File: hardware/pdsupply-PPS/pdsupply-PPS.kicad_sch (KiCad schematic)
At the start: 36 parts

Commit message: added a buck boost
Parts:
- removed C?: 0.1uF, symbol Device:C_Small
- removed C?: 10uF X5R 0805, symbol Device:C_Small
- removed C? (x4): 1uF, symbol Device:C_Small
- removed C? (x2): 12pF, symbol Device:C_Small
- removed Q?: STL6P3LLH6, TRANS_STL6P3LLH6, symbol STL6P3LLH6:STL6P3LLH6
- removed R?: 100, symbol Device:R_Small_US
- removed R? (x3): 100k, symbol Device:R_Small_US
- removed R? (x2): 1K, symbol Device:R_Small_US
- removed R?: 76.8k, symbol Device:R_Small_US
- removed R?: 22K, symbol Device:R_Small_US
- removed R?: 23.7k, symbol Device:R_Small_US
- removed U?: STUSB4500QTR, Package_DFN_QFN:QFN-24-1EP_4x4mm_P0.5mm_EP2.7x2.7mm, symbol Interface_USB:STUSB4500QTR
- removed U?: LTM8074IY, BGA25C65P5X5_400X400X198N, symbol LTM8074IY_PBF:LTM8074IY#PBF_MIRRORED
- removed Y?: Crystal, symbol Device:Crystal_GND24
- added C?: 22uF, symbol Device:C_Polarized_Small
- added C? (x2): 0.1uF, symbol Device:C_Small
- added C? (x3): 10uF, symbol Device:C_Small
- added FB? (x2): 1000Ω AT 100MHz, symbol Device:FerriteBead_Small
- added FB?: 300Ω AT 100MHz, symbol Device:FerriteBead_Small
- added IC?: FPF2895UCX, BGA24C40P4X6_167X260X61, symbol FPF2895UCX:FPF2895UCX
- added IC?: LTM8083EY#PBF, BGA49C80P7X7_625X625X242, symbol LTM8083EY#PBF:LTM8083EY#PBF
- added JP? (x2): Jumper_2_Open, symbol Jumper:Jumper_2_Open
- added R?: 200k, symbol Device:R_Small_US
- added R?: 22k, symbol Device:R_Small_US
- added R?: 50.6k, symbol Device:R_Small_US
- added R?: 270k, symbol Device:R_Small_US
- added R?: 40.2k, symbol Device:R_Small_US
- added U?: FUSB307BMPX, Package_DFN_QFN:WQFN-16-1EP_3x3mm_P0.5mm_EP1.75x1.75mm, symbol Interface_USB:FUSB307BMPX
- added X?: XO91, Oscillator:Oscillator_SMD_EuroQuartz_XO91-4Pin_7.0x5.0mm, symbol Oscillator:XO91
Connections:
- net +3V3: now also D?.1 (VDD), D?.1 (VDD), C?.1, FB?.2, X?.1 (EN), X?.4 (V+)
- net GND: now also D?.6 (GND), D?.6 (GND), C?.2, C?.2, C?.2, C?.2, C?.2, C?.2, IC?.A1 (GND_1), IC?.A2 (GND_2), IC?.A3 (GND_3), IC?.A7 (TST2), IC?.B1 (GND_4), IC?.B2 (GND_5), IC?.B3 (GND_6), IC?.B7 (OVLO), IC?.C1 (GND_7), IC?.C2 (GND_8), IC?.C3 (GND_9), IC?.C4 (GND_10), IC?.C5 (GND_11), IC?.D1 (GND_12), IC?.D2 (GND_13), IC?.D3 (GND_14), IC?.D4 (GND_15), IC?.D5 (GND_16), IC?.D7 (GND_17), IC?.E1 (GND_18), IC?.E2 (GND_19), IC?.E3 (GND_20), IC?.E4 (GND_21), IC?.E5 (GND_22), IC?.F1 (GND_23), IC?.F2 (GND_24), IC?.G1 (GND_25), IC?.G2 (GND_26), IC?.G6 (SYNC), R?.2, R?.2, R?.2, X?.2 (GND)
- net VBUS: now also C?.1, C?.1, FB?.1, FB?.1
- net at R?.2, U?.7 (UD+): now also JP?.1 (A)
- net SPI1_DATA: now reaches U?.13 (PA7)
- net SPI1_DATA: now also D?.4 (SDI)
- net USB_DM: now reaches U?.21 (PA11)
- net USB_DM: now also U?.11 (DD-), JP?.2 (B)
- net USB_DP: now reaches U?.22 (PA12)
- net USB_DP: now also U?.10 (DD+), JP?.2 (B)
- net SPI3_CLK: now reaches U?.26 (PB3)
- net SPI3_CLK: now also D?.5 (CKI)
- net SPI3_DATA: now reaches U?.28 (PB5)
- net SPI3_DATA: now also D?.4 (SDI)
- net at U?.6 (PA0): now also X?.3 (OUT)
- net SPI1_CLK: now reaches U?.7 (PA1)
- net SPI1_CLK: now also D?.5 (CKI)
- net at R?.1, U?.6 (UD-): now also JP?.1 (A)
- new net: C?.1, C?.1, FB?.2, FB?.2, IC?.A4 (VIN_1), IC?.A5 (VIN_2), IC?.A6 (SVIN), IC?.B4 (VIN_3), IC?.B5 (VIN_4), R?.1
- new net: IC?.B6 (EN/UVLO), R?.1, R?.2
- new net: U?.15 (GND), U?.17 (GND)
- new net: IC?.F7 (FB), R?.1, R?.2
- new net: C?.1, FB?.1, IC?.F3 (ISN), IC?.F4 (VOUT_1), IC?.F5 (VOUT_2), IC?.G3 (ISP), IC?.G4 (VOUT_3), IC?.G5 (VOUT_4), R?.1
- new net: IC?.E7 (RT), R?.1
- no-connect marks 19 -> 20
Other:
- note added: "Compliant with CISPR25 Class 5 Limits"
- moved on the sheet: C?, D?, PH?, R?, U?

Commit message: minor changes
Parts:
- removed D? (x2): APA102-2020, LED_SMD:LED-APA102-2020, symbol LED:APA102-2020
- removed X?: XO91, Oscillator:Oscillator_SMD_EuroQuartz_XO91-4Pin_7.0x5.0mm, symbol Oscillator:XO91
- added D? (x2): 25V, symbol Device:D_Schottky_Small
- added R? (x2): 5.1k, symbol Device:R_Small_US
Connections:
- net CC1: now also D?.1 (K)
- net CC2: now also D?.1 (K)
- net GND: now also D?.2 (A), D?.2 (A), R?.2, R?.2
- net CC1_PC: now reaches J?.A5 (CC1)
- net CC1_PC: now also R?.1
- net CC2_PC: now reaches J?.B5 (CC2)
- net CC2_PC: now also R?.1
- net SPI3_CLK: no longer names the net of U?.26 (PB3)
- net SPI3_DATA: no longer names the net of U?.28 (PB5)
- no-connect marks 20 -> 18
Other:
- moved on the sheet: R?, U?

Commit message: SCH 90% done
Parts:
- added C?: 0.1uF, symbol Device:C_Small
- added C? (x2): 220pF, symbol Device:C_Small
- added C?: 10uF, symbol Device:C_Small
- added C? (x2): 1uF, symbol Device:C_Small
- added D? (x2): LED_Small, symbol Device:LED_Small
- added D?: Led1, symbol Device:LED_Small
- added R? (x3): 4.7k, symbol Device:R_Small_US
- added R?: 890, symbol Device:R_Small_US
- added R? (x3): 10k, symbol Device:R_Small_US
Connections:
- net +3V3: now also U?.7 (VDD), C?.1, C?.1, D?.2 (A), R?.2, R?.2, R?.2
- net +5V: now also D?.2 (A)
- net CC1: now also U?.1 (CC1), C?.1
- net CC2: now also U?.3 (CC2), C?.1
- net GND: now also IC?.A4 (POL), IC?.B1 (GND_1), IC?.B2 (OC_M_ODE), IC?.B3 (OV1), IC?.B4 (GND_2), IC?.C4 (OV2), U?.15 (GND), U?.17 (GND), U?.4 (ORIENT/I2C_ADDR), C?.2, C?.2, C?.2, C?.2, C?.2, C?.2, R?.2, R?.2, R?.2, R?.2
- net VBUS: now also IC?.C3 (VIN_1), IC?.D3 (VIN_2), IC?.D4 (VIN_3), IC?.E3 (VIN_4), IC?.E4 (VIN_5), IC?.F3 (VIN_6), IC?.F4 (VIN_7), U?.6 (VBUS), C?.1
- net ON: now reaches IC?.A2 (ON)
- net ON: now also U?.14 (PB0)
- net FLAGB: now reaches IC?.A3 (FLAGB)
- net FLAGB: now also U?.15 (PB1)
- net at IC?.C1 (ISET): now also R?.1
- net VS: now reaches IC?.C2 (VOUT_1)
- net VS: now also IC?.D1 (VOUT_2), IC?.D2 (VOUT_3), IC?.E1 (VOUT_4), IC?.E2 (VOUT_5), IC?.F1 (VOUT_6), IC?.F2 (VOUT_7), C?.1
- net INT_N: now reaches U?.10 (INT_N)
- net INT_N: now also U?.18 (PA8), R?.1
- net SCL: now reaches U?.11 (SCL1/SDA2)
- net SCL: now also U?.19 (PA9), R?.1
- net SDA: now reaches U?.12 (SDA1/SCL2)
- net SDA: now also U?.20 (PA10), R?.1
- net at U?.26 (PB3): now also D?.2 (A)
- net SPI1_CLK: no longer names the net of U?.7 (PA1)
- net SPI1_DATA: no longer names the net of U?.13 (PA7)
- new net: D?.1 (K), R?.1 (x3)
- no-connect marks 18 -> 20
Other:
- note removed: "SPD Pin = Speed Select, Downstream Buffer. Active high logic input. When SPD is tied high, the full speed slew rate, timing, and logic conventions are selected; when SPD is tied low, the low speed slew rate, timing, and logic conventions are selected. This input must be set high via connection to VDD2 or set low via connection to GND2 and must match Pin 5 (both pins tied high or both pins tied lo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"
- note removed: "https://e2e.ti.com/cfs-file/__key/communityserver-discussions-components-files/138/2018_2D00_05_2D00_30-12_2D00_48_2D00_52.jpg Tusb422 Ref design"
- moved on the sheet: C?, D?, FB?, IC?, J?, JP?, PH?, R?, U?

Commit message: adj
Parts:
- added D? (x2): 25V, symbol Device:D_Schottky_Small
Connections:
- net CC1_PC: now also D?.1 (K)
- net CC2_PC: now also D?.1 (K)
- net GND: now also D?.2 (A), D?.2 (A)
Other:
- moved on the sheet: C?, D?, R?

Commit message: cleaned up SCH
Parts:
- added C?: Decide, symbol Device:C_Small
- added C?: .1uF, symbol Device:C_Small
- added U?: ACS71240KEXBLT-050U5, XDCR_ACS71240KEXBLT-050U5, symbol ACS71240KEXBLT-050U5:ACS71240KEXBLT-050U5
- R? (x3): value 4.7k -> 1k
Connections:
- net +3V3: now also C?.1, U?.12 (VCC)
- net GND: now also C?.2, C?.2, U?.5 (GND)
- net VS: now also U?.3 (IP-); no longer C?.1, IC?.C2 (VOUT_1), IC?.D1 (VOUT_2), IC?.D2 (VOUT_3), IC?.E1 (VOUT_4), IC?.E2 (VOUT_5), IC?.F1 (VOUT_6), IC?.F2 (VOUT_7)
- net SenseFault: now reaches U?.13 (PA7)
- net SenseFault: now also U?.6 (~{FAULT})
- new net: C?.1, IC?.C2 (VOUT_1), IC?.D1 (VOUT_2), IC?.D2 (VOUT_3), IC?.E1 (VOUT_4), IC?.E2 (VOUT_5), IC?.F1 (VOUT_6), IC?.F2 (VOUT_7), U?.1 (IP+)
- new net: U?.10 (NC), U?.7 (NC), U?.8 (NC), U?.9 (NC)
- new net Isense: C?.1, U?.11 (VIOUT)
- no-connect marks 20 -> 21
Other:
- moved on the sheet: C?, D?, FB?, IC?, J?, JP?, PH?, R?, U?

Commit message: SCH done
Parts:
- removed C?: Decide, symbol Device:C_Small
- added TP? (x16): RCU-0C, TP+195X110, symbol RCU-0C:RCU-0C
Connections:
- net +3V3: now also TP?.1
- net +5V: now also TP?.1
- net CC1: now also TP?.1
- net CC2: now also TP?.1
- net FLAGB: now also TP?.1
- net GND: no longer R?.2
- net GND1: now also R?.2
- net INT_N: now also TP?.1
- net Isense: now also U?.6 (PA0), TP?.1
- net ON: now also TP?.1
- net SCL: now also TP?.1
- net SDA: now also TP?.1
- net SenseFault: now also TP?.1
- net USB_DM: now also TP?.1
- net USB_DP: now also TP?.1
- net at JP?.1 (A), R?.2, U?.7 (UD+): now also TP?.1
- net DBG_N: now reaches U?.8 (DBG_N)
- net DBG_N: now also U?.12 (PA6), TP?.1
- net at JP?.1 (A), R?.1, U?.6 (UD-): now also TP?.1
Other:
- moved on the sheet: C?, D?, JP?, R?, U?

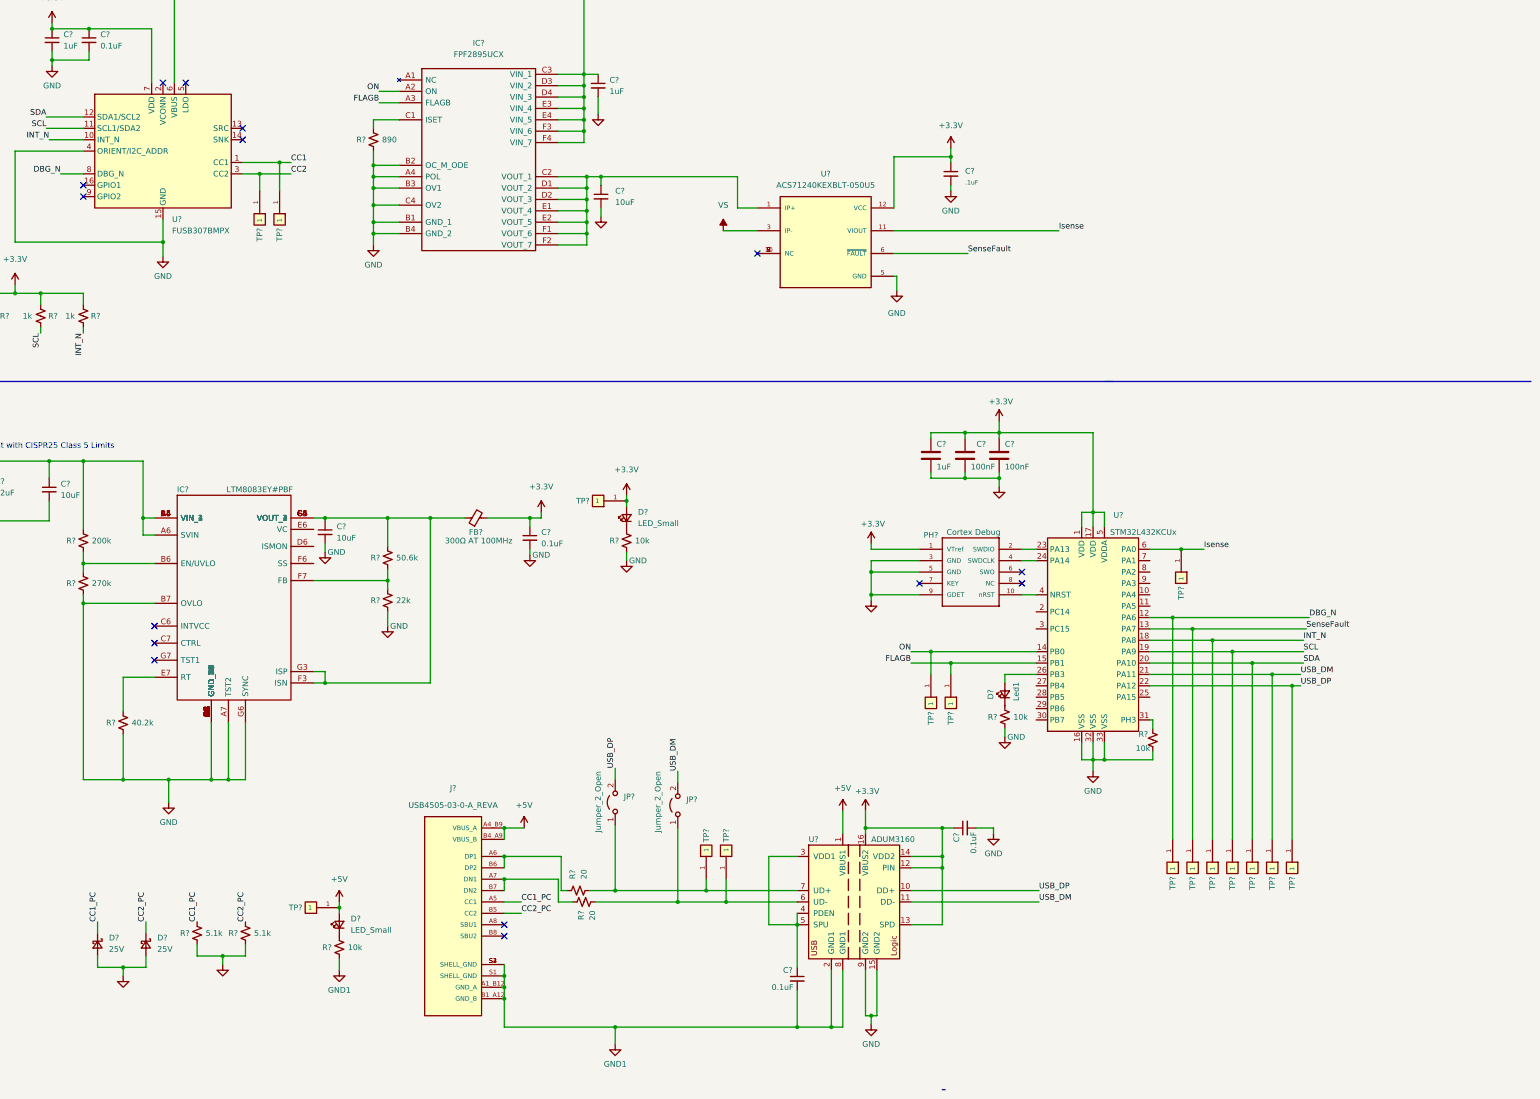
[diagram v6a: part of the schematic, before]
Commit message: Changed SW Conn
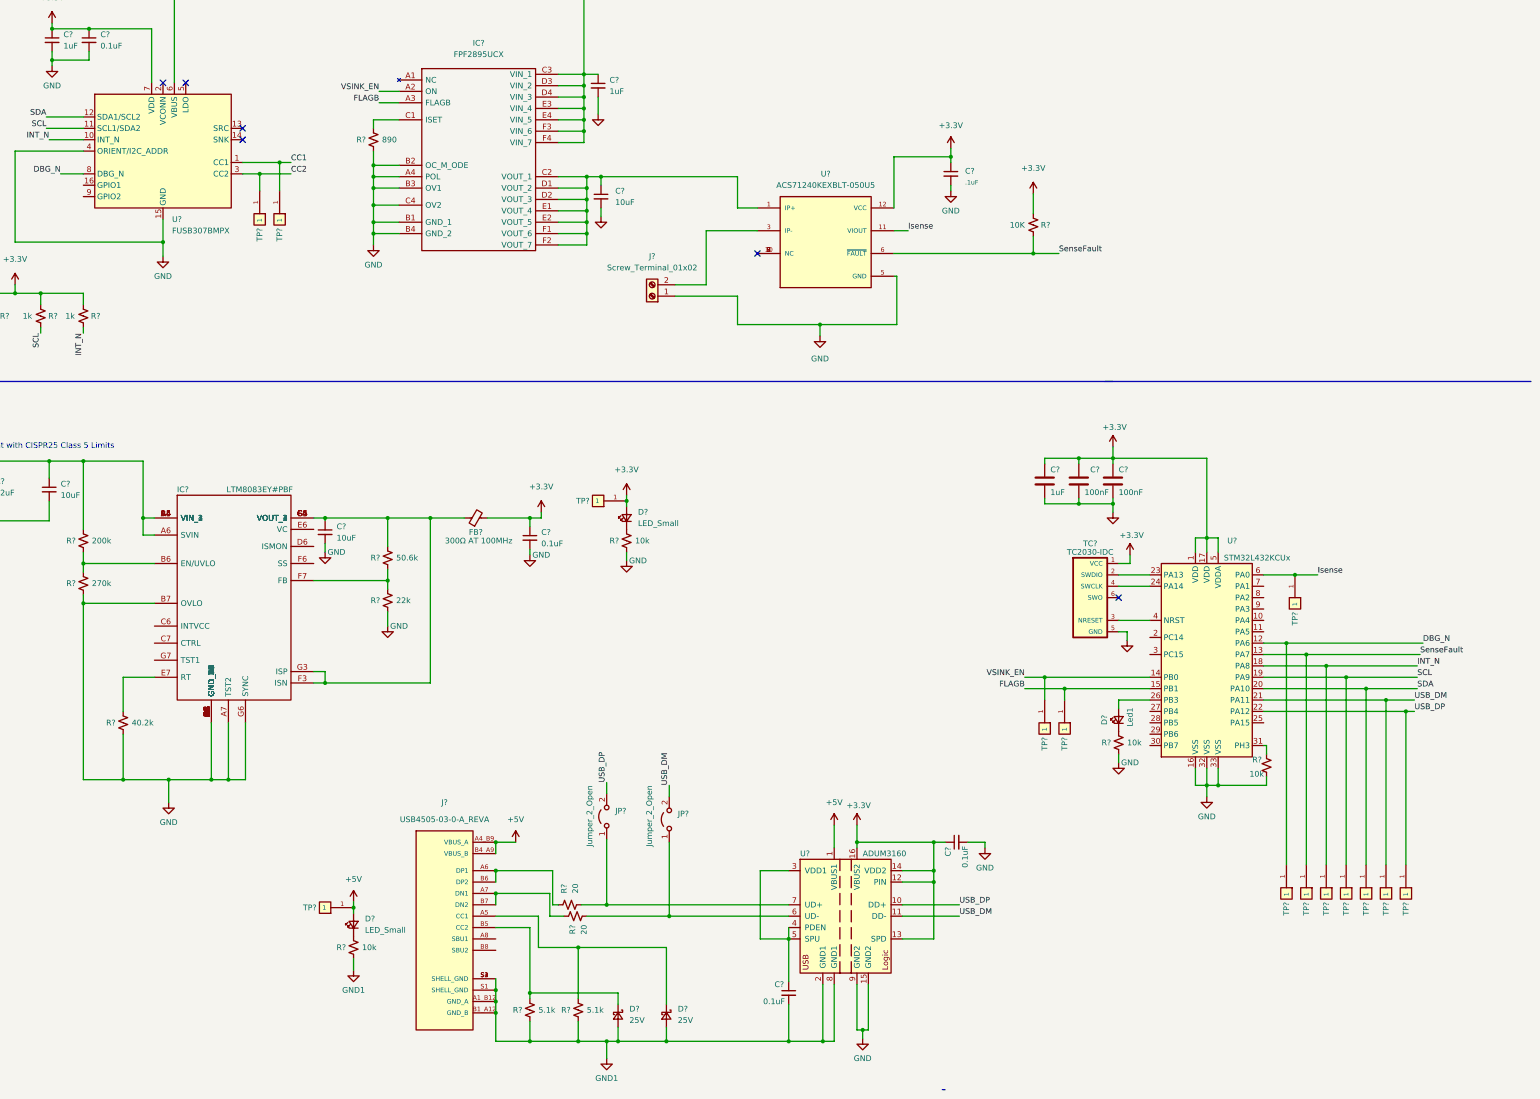
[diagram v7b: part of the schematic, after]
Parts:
- removed PH?: FTSH-105-01-L-DV-K, FTSH-105-01-L-DV-K:SAMTEC_FTSH-105-01-L-DV-K, symbol FTSH-105-01-L-DV-K:FTSH-105-01-L-DV-K
- removed TP? (x2): RCU-0C, TP+195X110, symbol RCU-0C:RCU-0C
- added J?: Screw_Terminal_01x02, symbol Connector:Screw_Terminal_01x02
- added R?: 10K, symbol Device:R_Small_US
- added TC?: TC2030-IDC, symbol TC2030-IDC:TC2030-IDC
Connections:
- net +3V3: now also R?.2, TC?.1 (VCC)
- net GND: now also J?.1 (Pin_1), TC?.5 (GND); no longer D?.2 (A), D?.2 (A), R?.2, R?.2
- net GND1: now also D?.2 (A), D?.2 (A), R?.2, R?.2
- net SenseFault: now also R?.1
- net at U?.23 (PA13): now also TC?.2 (SWDIO)
- net at U?.24 (PA14): now also TC?.4 (SWCLK)
- net at U?.4 (NRST): now also TC?.3 (NRESET)
- net CC1_PC: no longer names the net of D?.1 (K), R?.1
- net CC1_PC: now also J?.B5 (CC2); no longer J?.A5 (CC1)
- net CC2_PC: no longer names the net of D?.1 (K), R?.1
- net CC2_PC: now also J?.A5 (CC1); no longer J?.B5 (CC2)
- net ON renamed VSINK_EN
- net VS: no longer names the net of U?.3 (IP-)
- net VS: now also J?.2 (Pin_2)
- no-connect marks 21 -> 12
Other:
- moved on the sheet: C?, D?, J?, JP?, R?, TP?, U?

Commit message: FB assigned , started component placements
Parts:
- removed C?: 22uF, symbol Device:C_Polarized_Small
- added GPIO1, GPIO2: RCU-0C, RCU-0C:TP+195X110, symbol RCU-0C:RCU-0C
- added R17: 10k, Resistor_SMD:R_0603_1608Metric, symbol Device:R_Small_US
- +3.3V1, +5V1, CC1, CC2, DBG_N1, FLAGB1, INT_N1, Isense1, SCL1, SDA1, SenseFault1, USB_DM1, USB_DP1, VSINK_EN1: renamed from TP?; footprint TP+195X110 -> RCU-0C:TP+195X110
- C1, C11, C12, C13, C14, C18, C4, C5, C7, C9: renamed from C?; footprint (none) -> Capacitor_SMD:C_0603_1608Metric
- C10: renamed from C?; footprint (none) -> Capacitor_SMD:C_0805_2012Metric
- C2, C6: renamed from C?; footprint (none) -> Capacitor_SMD:C_1206_3216Metric
- C8: renamed from C?; footprint (none) -> Capacitor_SMD:C_1210_3225Metric
- D1, D2, D4, D6: renamed from D?; footprint (none) -> Diode_SMD:D_0603_1608Metric
- D3, D5, D7: renamed from D?; footprint (none) -> LED_SMD:LED_0603_1608Metric
- FB1, FB2, FB3: renamed from FB?; footprint (none) -> Inductor_SMD:L_0805_2012Metric
- IC1: renamed from IC?; footprint BGA49C80P7X7_625X625X242 -> ltm8083:BGA49C80P7X7_625X625X242
- IC2: renamed from IC?; footprint BGA24C40P4X6_167X260X61 -> FPF2895:BGA24C40P4X6_167X260X61
- J1, J2: renamed from J?; footprint GCT_USB4505-03-0-A_REVA -> USB4505-03-0-A_REVA:GCT_USB4505-03-0-A_REVA
- J3: renamed from J?; footprint (none) -> TerminalBlock_Phoenix:TerminalBlock_Phoenix_MKDS-1,5-2_1x02_P5.00mm_Horizontal
- JP1, JP2: renamed from JP?; footprint (none) -> Jumper:SolderJumper-2_P1.3mm_Open_TrianglePad1.0x1.5mm
- R1, R10, R11, R12, R13, R15, R18, R19, R2, R3, R4, R5, R6, R8, R9: renamed from R?; footprint (none) -> Resistor_SMD:R_0603_1608Metric
- R14, R16: renamed from R?; value 10k -> 200; footprint (none) -> Resistor_SMD:R_0603_1608Metric
- R7: renamed from R?; value 10k -> 350; footprint (none) -> Resistor_SMD:R_0603_1608Metric
- TC1: renamed from TC?; footprint (none) -> TC2030-IDC:TC2030-IDC
- U3: renamed from U?; footprint XDCR_ACS71240KEXBLT-050U5 -> ACS71240KEXBLT-050U5:XDCR_ACS71240KEXBLT-050U5
- gave numbers to parts that had none: 6
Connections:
- net +3V3: now also R17.1
- net CC1: now also C5.1, D2.1 (K); no longer C4.1, D1.1 (K)
- net CC2: now also C4.1, D1.1 (K); no longer C5.1, D2.1 (K)
- net DBG_N: now also DBG_N1.1; no longer USB_DP1.1
- net GND: now also IC2.A1 (NC)
- net INT_N: now also INT_N1.1; no longer SDA1.1
- net SDA: now also SDA1.1; no longer INT_N1.1
- net SenseFault: now also SenseFault1.1; no longer USB_DM1.1
- net USB_DM: now also USB_DM1.1; no longer SenseFault1.1
- net USB_DP: now also USB_DP1.1; no longer DBG_N1.1
- net at U1.16 (GPIO1): now also GPIO1.1
- net at U1.9 (GPIO2): now also GPIO2.1
- net at TC1.3 (NRESET), U4.4 (NRST): now also R17.2
- no-connect marks 12 -> 32
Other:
- moved on the sheet: C12, C13, C18, C4, C5, C7, C8, C9, CC1, CC2, D1, D2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
